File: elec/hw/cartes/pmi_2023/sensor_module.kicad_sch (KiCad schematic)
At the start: 7 parts, among them U12 LSM6DSO32XTR

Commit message: wip
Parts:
- added C51, C53, C54, C56: 100nF 50V, symbol cocotter_capacitors:C_100nF_50V_0603
- added C52, C55: 10µF 16V, symbol cocotter_capacitors:C_10µF_16V_0805
- added R123, R124, R128: 10k, cocotter_resistor:r0603_reflow, symbol cocotter_resistors:R_10k_0603_1%
- added R125, R126, R129, R130: 100k, cocotter_resistor:r0603_reflow, symbol cocotter_resistors:R_100k_0603_1%
- added U22, U30: VL53L5CXV0GC, cocotter_ic:VL53L5CX, symbol cocotter_ic:VL53L5CXV0GC
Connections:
- net gyro_irq_3v3: now reaches R38.2, U12.4 (INT1)
- new net: R129.2, R130.2, U30.C2 (RSVD6)
- new net +3.3V: C51.1, C52.1, C53.1, C54.1, C55.1, C56.1, R123.1, R125.1, R126.1, R129.1, R130.1, U22.A4 (IOVDD), U22.B1 (AVDD), U22.B7 (AVDD), U30.A4 (IOVDD), U30.B1 (AVDD), U30.B7 (AVDD)
- new net GND: C51.2, C52.2, C53.2, C54.2, C55.2, C56.2, R124.2, R128.2, U22.A2 (RSVD4), U22.A6 (RSVD1), U22.A7 (RSVD2), U22.B4 (THERM_PAD), U22.C1 (GND), U22.C6 (RSVD3), U22.C7 (GND), U30.A2 (RSVD4), U30.A6 (RSVD1), U30.A7 (RSVD2), U30.B4 (THERM_PAD), U30.C1 (GND), U30.C6 (RSVD3), U30.C7 (GND)
- new net VL53L5_I2C_RST_u22_3v3: R124.1, U22.A1 (I2C_RST)
- new net VL53L5_I2C_RST_u30_3v3: R128.1, U30.A1 (I2C_RST)
- new net enable_next_tof_sensor_3v3: R125.2, R126.2, U22.C2 (RSVD6), U30.A5 (LPn)
- new net enable_tof_3v3: U22.A5 (LPn)
- new net scl_3v3: U22.C4 (SCL), U30.C4 (SCL)
- new net sda_3v3: U22.C3 (SDA), U30.C3 (SDA)
- new net tof_irq: R123.2, U22.A3 (INT), U30.A3 (INT)
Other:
- note removed: "TODO gerer IRQ"
- moved on the sheet: C12, R101, R38, R39, R44, R45, U12

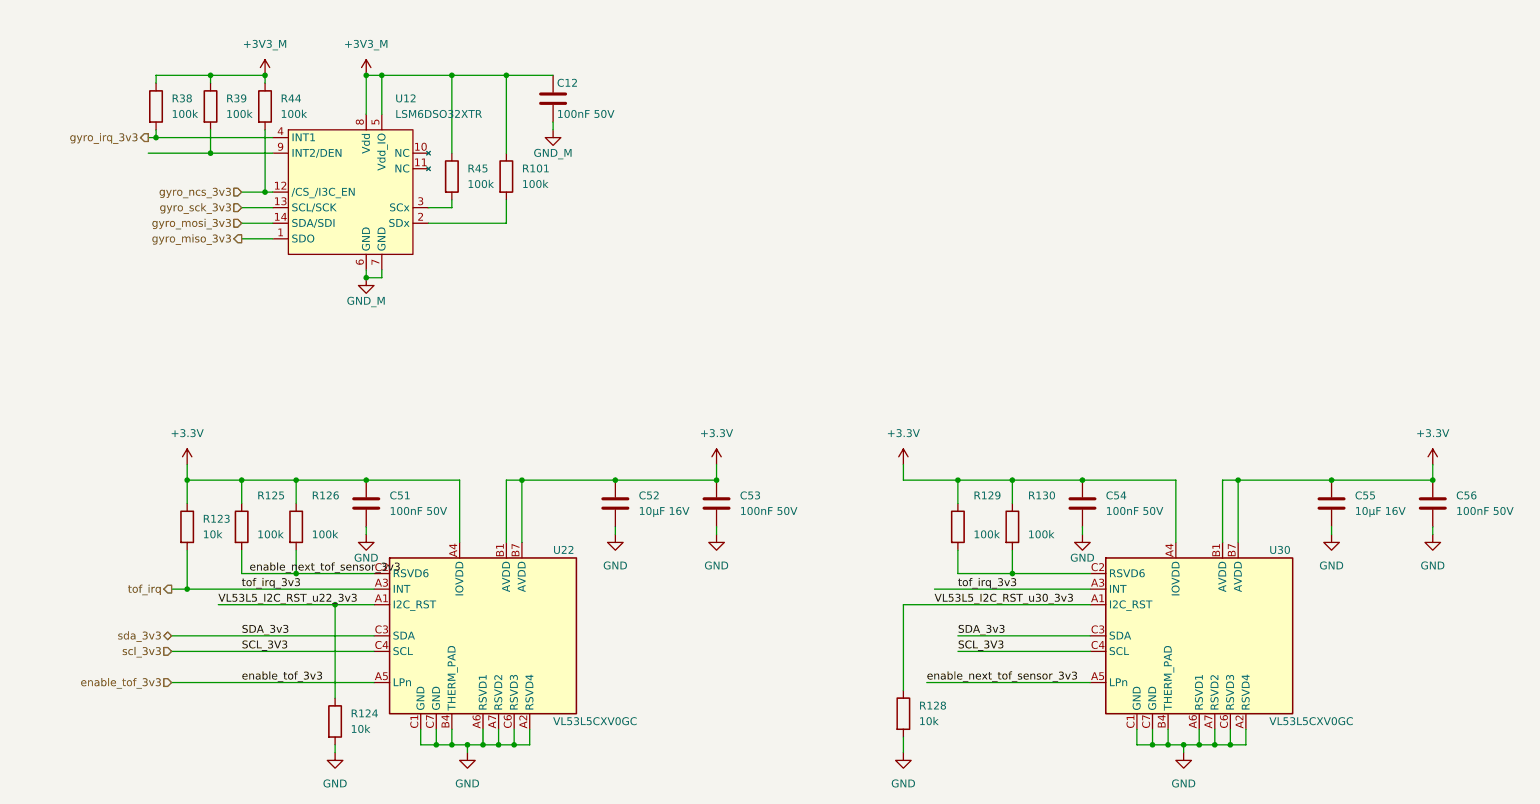
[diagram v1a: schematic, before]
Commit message: front and back tof added, selector changed, ready to route
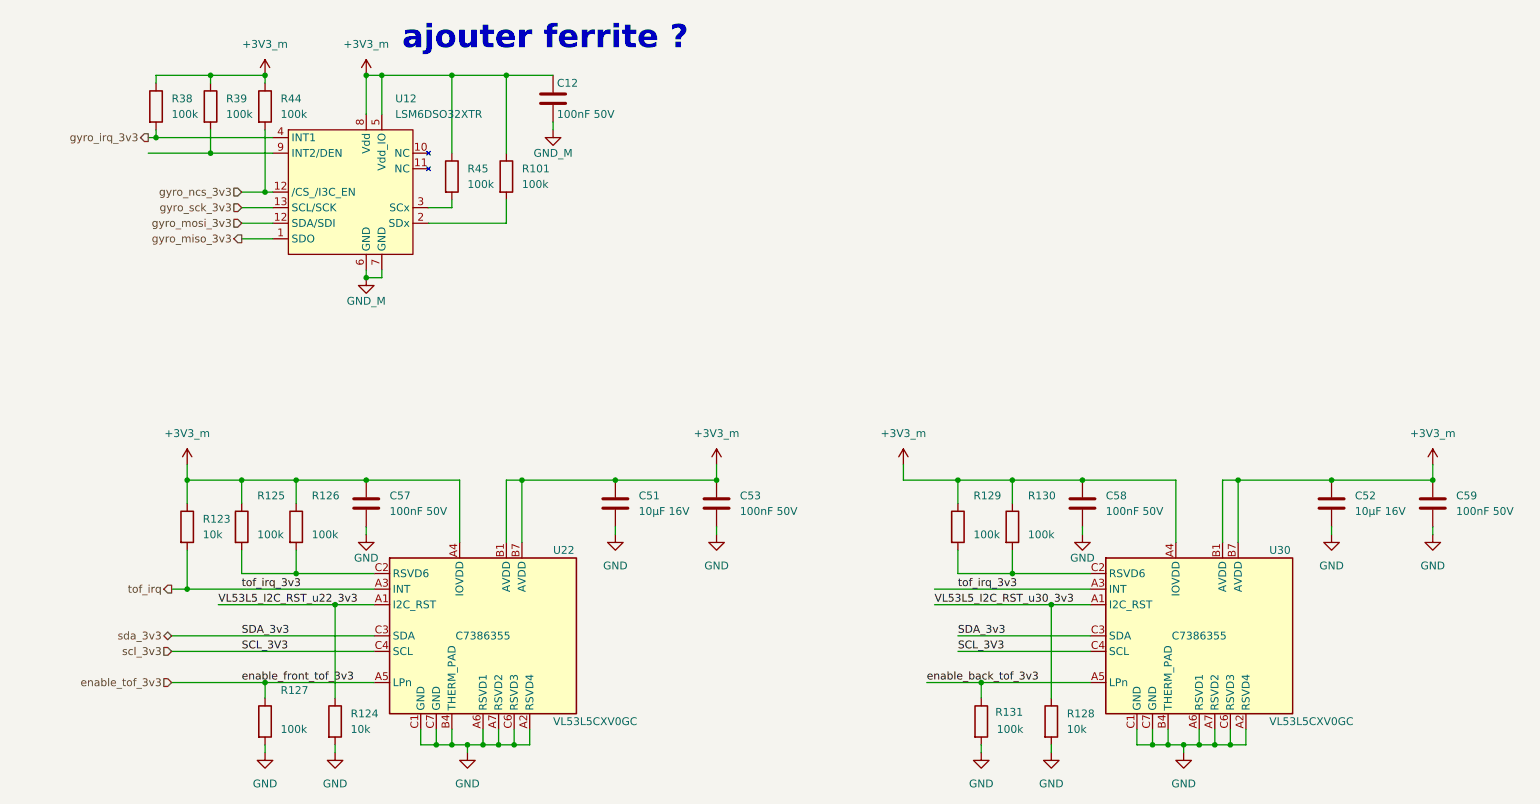
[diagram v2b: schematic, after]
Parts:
- removed C51, C54, C56: 100nF 50V, symbol cocotter_capacitors:C_100nF_50V_0603
- removed C55: 10µF 16V, symbol cocotter_capacitors:C_10µF_16V_0805
- added C51: 10µF 16V, cocotter_capacitors:C_0805_2012Metric, symbol cocotter_capacitors:C_10µF_16V_0805
- added C57, C58, C59: 100nF 50V, cocotter_capacitors:C_0603_1608Metric, symbol cocotter_capacitors:C_100nF_50V_0603
- added R127, R131: 100k, cocotter_resistor:r0603_reflow, symbol cocotter_resistors:R_100k_0603_1%
- C52: footprint (none) -> cocotter_capacitors:C_0805_2012Metric
- C53: footprint (none) -> cocotter_capacitors:C_0603_1608Metric
- U22, U30: JLCPCB (none) -> C7386355
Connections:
- net +3.3V is gone; now on net +3V3_m: C52.1, C53.1, R123.1, R125.1, R126.1, R129.1, R130.1, U22.A4 (IOVDD), U22.B1 (AVDD), U22.B7 (AVDD), U30.A4 (IOVDD), U30.B1 (AVDD), U30.B7 (AVDD)
- net +3V3_m: now also C51.1, C57.1, C58.1, C59.1
- net GND: now also C51.2, C57.2, C58.2, C59.2, R127.2, R131.2
- net enable_tof_3v3: now also R127.1
- net gyro_mosi_3v3: now also U12.12 (SDA/SDI); no longer U12.14 (SDA/SDI)
- net enable_next_tof_sensor_3v3: no longer names the net of R125.2, R126.2, U22.C2 (RSVD6)
- net enable_next_tof_sensor_3v3: no longer U30.A5 (LPn)
- new net enable_back_tof_3v3: R131.1, U30.A5 (LPn)
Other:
- note added: "ajouter ferrite ?"
- moved on the sheet: R128

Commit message: corrected librariesand ongoing routing
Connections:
- net gyro_mosi_3v3: now also U12.14 (SDA/SDI); no longer U12.12 (SDA/SDI)
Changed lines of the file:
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@@
 			)
 		)
-		(property "Description" ""
+		(property "Description" "Resistor"
 			(at 52.07 27.94 0)
 			(effects
@@
 		(pin "11"
 		)
+		(pin "14"
+		)
 		(pin "12"
-		)
-		(pin "12"

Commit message: wip
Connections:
- net GND is gone; now on net GND_M: C51.2, C52.2, C53.2, C57.2, C58.2, C59.2, R124.2, R127.2, R128.2, R131.2, U22.A2 (RSVD4), U22.A6 (RSVD1), U22.A7 (RSVD2), U22.B4 (THERM_PAD), U22.C1 (GND), U22.C6 (RSVD3), U22.C7 (GND), U30.A2 (RSVD4), U30.A6 (RSVD1), U30.A7 (RSVD2), U30.B4 (THERM_PAD), U30.C1 (GND), U30.C6 (RSVD3), U30.C7 (GND)
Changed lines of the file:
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@@
 			)
 		)
-		(property "Value" "GND"
+		(property "Value" "GND_M"
 			(at 242.57 102.87 0)
 			(effects
@@
 			)
 		)
-		(property "Description" ""
+		(property "Description" "Power symbol creates a global label with name \"GND\" , ground"
 			(at 242.57 97.79 0)
 			(effects
@@
 			)
 		)
-		(property "Description" ""
+		(property "Description" "Resistor"
 			(at 82.55 39.37 0)
 			(effects
@@
 			)
 		)
-		(property "Description" ""
+		(property "Description" "Power symbol creates a global label with name \"+3.3V\""
 			(at 39.37 86.36 0)
 			(effects
@@
 			)
 		)
-		(property "Description" ""
+		(property "Description" "Time-of-Flight 8x8 multizone ranging sensor with wide field of view"
 			(at 204.47 114.3 0)
 			(effects
@@
 			)
 		)
-		(property "Description" ""
+		(property "Description" "Power symbol creates a global label with name \"+3.3V\""
 			(at 242.57 86.36 0)
 			(effects
@@
 			)
 		)
-		(property "Description" ""
+		(property "Description" "Resistor"
 			(at 57.15 96.52 0)
 			(effects
@@
 			)
 		)
-		(property "Description" ""
+		(property "Description" "Power symbol creates a global label with name \"GND\" , ground"
 			(at 68.58 55.88 0)
 			(effects
@@
 			)
 		)
-		(property "Value" "GND"
+		(property "Value" "GND_M"
 			(at 125.73 102.87 0)
 			(effects
@@
 			)
 		)
-		(property "Description" ""
+		(property "Description" "Power symbol creates a global label with name \"GND\" , ground"
 			(at 125.73 97.79 0)
 			(effects
@@
 			)
 		)
-		(property "Value" "GND"
+		(property "Value" "GND_M"
 			(at 52.07 138.43 0)
 			(effects
@@
 			)
 		)
-		(property "Description" ""
+		(property "Description" "Power symbol creates a global label with name \"GND\" , ground"
 			(at 52.07 133.35 0)
 			(effects
@@
 			)
 		)
-		(property "Description" ""
+		(property "Description" "Resistor"
 			(at 173.99 96.52 0)
 			(effects
@@
 			)
 		)
-		(property "Description" ""
+		(property "Description" "Power symbol creates a global label with name \"+3.3V\""
 			(at 156.21 86.36 0)
 			(effects
@@
 			)
 		)
-		(property "Description" ""
+		(property "Description" "Power symbol creates a global label with name \"+3V3\""
 			(at 52.07 22.86 0)
 			(effects
@@
 			)
 		)
-		(property "Description" ""
+		(property "Description" "Power symbol creates a global label with name \"+3.3V\""
 			(at 125.73 86.36 0)
 			(effects
@@
 			)
 		)
-		(property "Value" "GND"
+		(property "Value" "GND_M"
 			(at 68.58 101.6 0)
 			(effects
@@
 			)
 		)
-		(property "Description" ""
+		(property "Description" "Power symbol creates a global label with name \"GND\" , ground"
 			(at 68.58 97.79 0)
 			(effects
@@
 			)
 		)
-		(property "Value" "GND"
+		(property "Value" "GND_M"
 			(at 226.06 102.87 0)
 			(effects
@@
 			)
 		)
-		(property "Description" ""
+		(property "Description" "Power symbol creates a global label with name \"GND\" , ground"
 			(at 226.06 97.79 0)
 			(effects
@@
 			)
 		)
-		(property "Description" ""
+		(property "Description" "Power symbol creates a global label with name \"GND\" , ground"
 			(at 99.06 31.75 0)
 			(effects
@@
 			)
 		)
-		(property "Value" "GND"
+		(property "Value" "GND_M"
 			(at 109.22 102.87 0)
 			(effects
@@
 			)
 		)
-		(property "Description" ""
+		(property "Description" "Power symbol creates a global label with name \"GND\" , ground"
 			(at 109.22 97.79 0)
 			(effects
@@
 			)
 		)
-		(property "Description" ""
+		(property "Description" "Resistor"
 			(at 91.44 39.37 0)
 			(effects
@@
 			)
 		)
-		(property "Description" ""
+		(property "Description" "Resistor"
 			(at 48.26 96.52 0)
 			(effects
@@
 			)
 		)
-		(property "Value" "GND"
+		(property "Value" "GND_M"
 			(at 180.34 138.43 0)
 			(effects
@@
 			)
 		)
-		(property "Description" ""
+		(property "Description" "Power symbol creates a global label with name \"GND\" , ground"
 			(at 180.34 133.35 0)
 			(effects
@@
 			)
 		)
-		(property "Description" ""
+		(property "Description" "Power symbol creates a global label with name \"+3V3\""
 			(at 68.58 22.86 0)
 			(effects
@@
 			)
 		)
-		(property "Description" ""
+		(property "Description" "Unpolarized capacitor"
 			(at 99.06 26.67 0)
 			(effects
@@
 			)
 		)
-		(property "Value" "GND"
+		(property "Value" "GND_M"
 			(at 85.09 138.43 0)
 			(effects
@@
 			)
 		)
-		(property "Description" ""
+		(property "Description" "Power symbol creates a global label with name \"GND\" , ground"
 			(at 85.09 133.35 0)
 			(effects
@@
 			)
 		)
-		(property "Description" ""
+		(property "Description" "Resistor"
 			(at 52.07 128.27 0)
 			(effects
@@
 			)
 		)
-		(property "Value" "GND"
+		(property "Value" "GND_M"
 			(at 168.91 138.43 0)
 			(effects
@@
 			)
 		)
-		(property "Description" ""
+		(property "Description" "Power symbol creates a global label with name \"GND\" , ground"
 			(at 168.91 133.35 0)
 			(effects
@@
 			)
 		)
-		(property "Value" "GND"
+		(property "Value" "GND_M"
 			(at 201.93 138.43 0)
 			(effects
@@
 			)
 		)
-		(property "Description" ""
+		(property "Description" "Power symbol creates a global label with name \"GND\" , ground"
 			(at 201.93 133.35 0)
 			(effects
@@
 			)
 		)
-		(property "Value" "GND"
+		(property "Value" "GND_M"
 			(at 63.5 138.43 0)
 			(effects
@@
 			)
 		)
-		(property "Description" ""
+		(property "Description" "Power symbol creates a global label with name \"GND\" , ground"
 			(at 63.5 133.35 0)
 			(effects
@@
 			)
 		)
-		(property "Description" ""
+		(property "Description" "Time-of-Flight 8x8 multizone ranging sensor with wide field of view"
 			(at 87.63 114.3 0)
 			(effects
@@
 			)
 		)
-		(property "Description" ""
+		(property "Description" "Resistor"
 			(at 168.91 128.27 0)
 			(effects
@@
 			)
 		)
-		(property "Description" ""
+		(property "Description" "Resistor"
 			(at 63.5 128.27 0)
 			(effects
@@
 			)
 		)
-		(property "Value" "GND"
+		(property "Value" "GND_M"
 			(at 185.42 101.6 0)
 			(effects
@@
 			)
 		)
-		(property "Description" ""
+		(property "Description" "Power symbol creates a global label with name \"GND\" , ground"
 			(at 185.42 97.79 0)
 			(effects
@@
 			)
 		)
-		(property "Description" ""
+		(property "Description" "Resistor"
 			(at 34.29 27.94 0)
 			(effects
@@
 			)
 		)
-		(property "Description" ""
+		(property "Description" "Resistor"
 			(at 165.1 96.52 0)
 			(effects
@@
 			)
 		)
-		(property "Description" ""
+		(property "Description" "Resistor"
 			(at 43.18 27.94 0)
 			(effects
@@
 			)
 		)
-		(property "Description" ""
+		(property "Description" "Resistor"
 			(at 39.37 96.52 0)
 			(effects
@@
 			)
 		)
-		(property "Description" ""
+		(property "Description" "Resistor"
 			(at 180.34 128.27 0)
 			(effects

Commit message: added oled display power supply res selectors, jlcpcb refs : wip
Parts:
- C51, C52: value 10µF 16V -> 10µF 25V; symbol cocotter_capacitors:C_10µF_16V_0805 -> cocotter_capacitors:C_10µF_25V_0805_X5R; JLCPCB (none) -> C15850; Specification 10µF 16V X7R 0805 -> 10µF 25V X7R 0805
- C53, C57, C58, C59: JLCPCB (none) -> C14663
- R123, R124, R128: value 10k -> 10k 1%; JLCPCB (none) -> C25804
- R125, R126, R127, R129, R130, R131: JLCPCB (none) -> C25803
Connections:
- net +3V3_m renamed +3.3V
- net +3.3V: no longer C12.1, R101.1, R38.1, R39.1, R44.1, R45.1, U12.5 (Vdd_IO), U12.8 (Vdd)
- net GND_M renamed GND
- new net +3V3: C12.1, R101.1, R38.1, R39.1, R44.1, R45.1, U12.5 (Vdd_IO), U12.8 (Vdd)
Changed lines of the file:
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@@
 	)
 	(symbol
-		(lib_id "cocotter_capacitors:C_10µF_16V_0805")
+		(lib_id "cocotter_capacitors:C_10µF_25V_0805_X5R")
 		(at 109.22 92.71 0)
 		(unit 1)
@@
 			)
 		)
-		(property "Value" "10µF 16V"
+		(property "Value" "10µF 25V"
 			(at 113.03 93.9799 0)
 			(effects
@@
 			)
 		)
-		(property "Specification" "10µF 16V X7R 0805 "
+		(property "Specification" "10µF 25V X7R 0805 "
 			(at 109.22 92.71 0)
 			(effects
@@
 			)
 		)
+		(property "JLCPCB" "C15850"
+			(at 109.22 92.71 0)
+			(effects
+				(font
+					(size 1.27 1.27)
+				)
+			)
+		)
 		(pin "1"
 		)
@@
 			)
 		)
-		(property "Description" "Unpolarized capacitor"
+		(property "Description" "Unpolarized capacitor tol +/-10%"
 			(at 68.58 92.71 0)
 			(effects
@@
 			)
 		)
+		(property "JLCPCB" "C14663"
+			(at 68.58 92.71 0)
+			(effects
+				(font
+					(size 1.27 1.27)
+				)
+			)
+		)
 		(pin "2"
 		)
@@
 			)
 		)
-		(property "Value" "GND_M"
+		(property "Value" "GND"
 			(at 242.57 102.87 0)
 			(effects
@@
 			)
 		)
-		(property "Description" "Unpolarized capacitor"
+		(property "Description" "Unpolarized capacitor tol +/-10%"
 			(at 185.42 92.71 0)
 			(effects
@@
 			)
 		)
+		(property "JLCPCB" "C14663"
+			(at 185.42 92.71 0)
+			(effects
+				(font
+					(size 1.27 1.27)
+				)
+			)
+		)
 		(pin "2"
 		)
@@
 			)
 		)
-		(property "Value" "+3V3_m"
+		(property "Value" "+3.3V"
 			(at 39.37 81.28 0)
 			(effects
@@
 			)
 		)
-		(property "Value" "+3V3_m"
+		(property "Value" "+3.3V"
 			(at 242.57 81.28 0)
 			(effects
@@
 			)
 		)
+		(property "JLCPCB" "C25803"
+			(at 57.15 96.52 0)
+			(effects
+				(font
+					(size 1.27 1.27)
+				)
+			)
+		)
 		(pin "1"
 		)
@@
 			)
 		)
-		(property "Value" "GND_M"
+		(property "Value" "GND"
 			(at 68.58 59.69 0)
 			(effects
@@
 			)
 		)
-		(property "Value" "GND_M"
+		(property "Value" "GND"
 			(at 125.73 102.87 0)
 			(effects
@@
 	)
 	(symbol
-		(lib_id "cocotter_capacitors:C_10µF_16V_0805")
+		(lib_id "cocotter_capacitors:C_10µF_25V_0805_X5R")
 		(at 226.06 92.71 0)
 		(unit 1)
@@
 			)
 		)
-		(property "Value" "10µF 16V"
+		(property "Value" "10µF 25V"
 			(at 229.87 93.9799 0)
 			(effects
@@
 			)
 		)
-		(property "Specification" "10µF 16V X7R 0805 "
+		(property "Specification" "10µF 25V X7R 0805 "
 			(at 226.06 92.71 0)
 			(effects
@@
 			)
 		)
+		(property "JLCPCB" "C15850"
+			(at 226.06 92.71 0)
+			(effects
+				(font
+					(size 1.27 1.27)
+				)
+			)
+		)
 		(pin "2"
 		)
@@
 			)
 		)
-		(property "Value" "GND_M"
+		(property "Value" "GND"
 			(at 52.07 138.43 0)
 			(effects
@@
 			)
 		)
-		(property "Description" "Unpolarized capacitor"
+		(property "Description" "Unpolarized capacitor tol +/-10%"
 			(at 242.57 92.71 0)
 			(effects
@@
 			)
 		)
+		(property "JLCPCB" "C14663"
+			(at 242.57 92.71 0)
+			(effects
+				(font
+					(size 1.27 1.27)
+				)
+			)
+		)
 		(pin "2"
 		)
@@
 			)
 		)
+		(property "JLCPCB" "C25803"
+			(at 173.99 96.52 0)
+			(effects
+				(font
+					(size 1.27 1.27)
+				)
+			)
+		)
 		(pin "1"
 		)
@@
 			)
 		)
-		(property "Value" "+3V3_m"
+		(property "Value" "+3.3V"
 			(at 156.21 81.28 0)
 			(effects
@@
 			)
 		)
-		(property "Value" "+3V3_m"
+		(property "Value" "+3V3"
 			(at 52.07 17.78 0)
 			(effects
@@
 			)
 		)
-		(property "Value" "+3V3_m"
+		(property "Value" "+3.3V"
 			(at 125.73 81.28 0)
 			(effects
@@
 			)
 		)
-		(property "Value" "GND_M"
+		(property "Value" "GND"
 			(at 68.58 101.6 0)
 			(effects
@@
 			)
 		)
-		(property "Description" "Unpolarized capacitor"
+		(property "Description" "Unpolarized capacitor tol +/-10%"
 			(at 125.73 92.71 0)
 			(effects
@@
 			)
 		)
+		(property "JLCPCB" "C14663"
+			(at 125.73 92.71 0)
+			(effects
+				(font
+					(size 1.27 1.27)
+				)
+			)
+		)
 		(pin "2"
 		)
@@
 			)
 		)
-		(property "Value" "GND_M"
+		(property "Value" "GND"
 			(at 226.06 102.87 0)
 			(effects
@@
 			)
 		)
-		(property "Value" "GND_M"
+		(property "Value" "GND"
 			(at 99.06 35.56 0)
 			(effects
@@
 			)
 		)
-		(property "Value" "GND_M"
+		(property "Value" "GND"
 			(at 109.22 102.87 0)
 			(effects
@@
 			)
 		)
+		(property "JLCPCB" "C25803"
+			(at 48.26 96.52 0)
+			(effects
+				(font
+					(size 1.27 1.27)
+				)
+			)
+		)
 		(pin "1"
 		)
@@
 			)
 		)
-		(property "Value" "GND_M"
+		(property "Value" "GND"
 			(at 180.34 138.43 0)
 			(effects
@@
 			)
 		)
-		(property "Value" "+3V3_m"
+		(property "Value" "+3V3"
 			(at 68.58 17.78 0)
 			(effects
@@
 			)
 		)
-		(property "Description" "Unpolarized capacitor"
+		(property "Description" "Unpolarized capacitor tol +/-10%"
 			(at 99.06 26.67 0)
 			(effects
@@
 			)
 		)
-		(property "Value" "GND_M"
+		(property "Value" "GND"
 			(at 85.09 138.43 0)
 			(effects
@@
 			)
 		)
+		(property "JLCPCB" "C25803"
+			(at 52.07 128.27 0)
+			(effects
+				(font
+					(size 1.27 1.27)
+				)
+			)
+		)
 		(pin "1"
 		)
@@
 			)
 		)
-		(property "Value" "GND_M"
+		(property "Value" "GND"
 			(at 168.91 138.43 0)
 			(effects
@@
 			)
 		)
-		(property "Value" "GND_M"
+		(property "Value" "GND"
 			(at 201.93 138.43 0)
 			(effects
@@
 			)
 		)
-		(property "Value" "GND_M"
+		(property "Value" "GND"
 			(at 63.5 138.43 0)
 			(effects
@@
 			)
 		)
+		(property "JLCPCB" "C25803"
+			(at 168.91 128.27 0)
+			(effects
+				(font
+					(size 1.27 1.27)
+				)
+			)
+		)
 		(pin "1"
 		)
@@
 			)
 		)
-		(property "Value" "10k"
+		(property "Value" "10k 1%"
 			(at 66.04 129.54 0)
 			(effects
@@
 			)
 		)
+		(property "JLCPCB" "C25804"
+			(at 63.5 128.27 0)
+			(effects
+				(font
+					(size 1.27 1.27)
+				)
+			)
+		)
 		(pin "1"
 		)
@@
 			)
 		)
-		(property "Value" "GND_M"
+		(property "Value" "GND"
 			(at 185.42 101.6 0)
 			(effects
@@
 			)
 		)
+		(property "JLCPCB" "C25803"
+			(at 165.1 96.52 0)
+			(effects
+				(font
+					(size 1.27 1.27)
+				)
+			)
+		)
 		(pin "1"
 		)
@@
 			)
 		)
-		(property "Value" "10k"
+		(property "Value" "10k 1%"
 			(at 41.91 97.79 0)
 			(effects
@@
 			)
 		)
+		(property "JLCPCB" "C25804"
+			(at 39.37 96.52 0)
+			(effects
+				(font
+					(size 1.27 1.27)
+				)
+			)
+		)
 		(pin "1"
 		)
@@
 			)
 		)
-		(property "Value" "10k"
+		(property "Value" "10k 1%"
 			(at 182.88 129.54 0)
 			(effects
@@
 			)
 		)
+		(property "JLCPCB" "C25804"
+			(at 180.34 128.27 0)
+			(effects
+				(font
+					(size 1.27 1.27)
+				)
+			)
+		)

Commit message: reset button added to esp32 reset. uart prog connector replaces ftdi one
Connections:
- net +3V3 is gone; now on net +3V3_m: C12.1, R101.1, R38.1, R39.1, R44.1, R45.1, U12.5 (Vdd_IO), U12.8 (Vdd)
- net +3.3V renamed +3V3_m
- net GND renamed GND_m
